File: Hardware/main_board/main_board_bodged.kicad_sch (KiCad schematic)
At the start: 116 parts, among them J1 ALARM, J2 RFID_CONN, J3 GPS_CONN, J4 USB_A, J5 DEBUG, J6 ANTENNA2, J7 Conn_01x04_Male, J8 BATT, SW1 SW_Push, SW2 SW_Push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

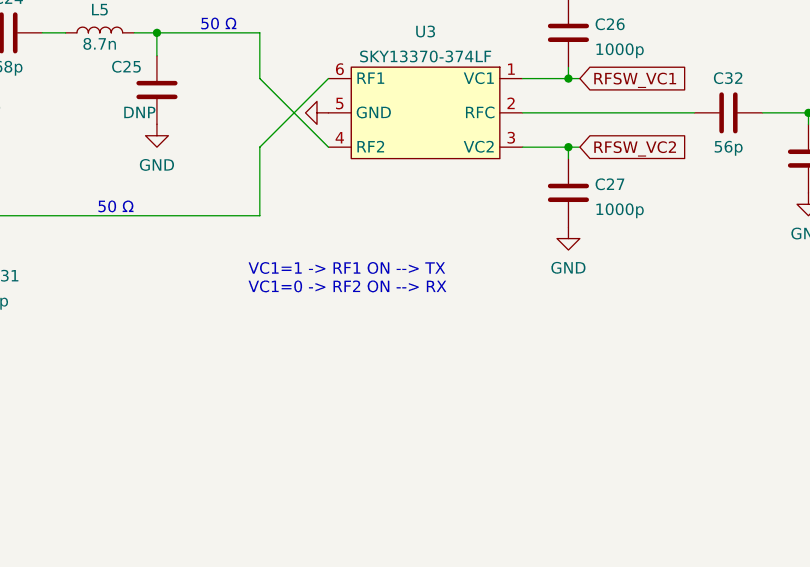
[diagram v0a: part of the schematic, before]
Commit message: lora helper functions
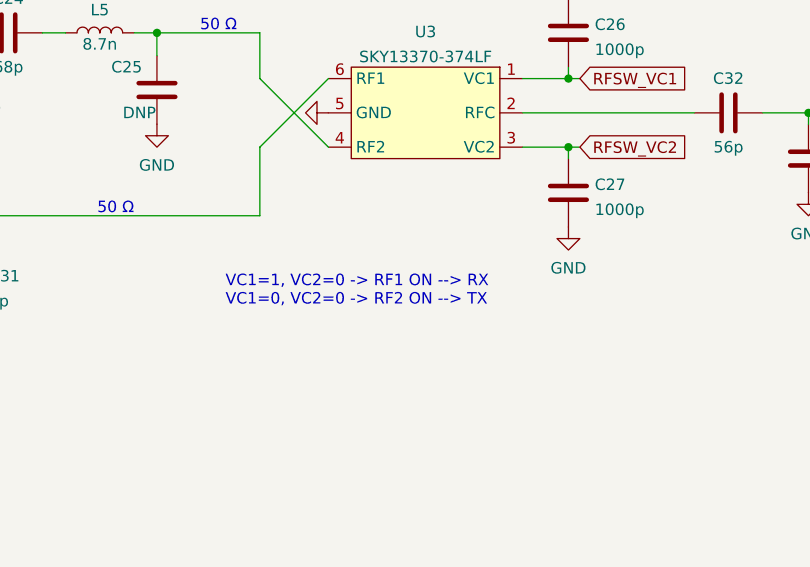
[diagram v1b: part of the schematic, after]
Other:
- note added: "VC1=1, VC2=0 -> RF1 ON --> RX VC1=0, VC2=0 -> RF2 ON --> TX"
- note removed: "VC1=1 -> RF1 ON --> TX VC1=0 -> RF2 ON --> RX"
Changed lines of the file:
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@@
     (effects (font (size 2 2) (thickness 0.4) bold italic) (justify left bottom))
   )
-  (text "VC1=1 -> RF1 ON --> TX \nVC1=0 -> RF2 ON --> RX\n" (at 190.5 114.3 0)
+  (text "VC1=1, VC2=0 -> RF1 ON --> RX\nVC1=0, VC2=0 -> RF2 ON --> TX\n"
+    (at 187.96 115.57 0)
     (effects (font (size 1.27 1.27)) (justify left bottom))
   )

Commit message: safety commit, uart working kinda
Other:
- note added: "PA8 (TP3): 32MHz master clock output"
- note added: "VC1=1, VC2=0 -> RF1 ON --> RX VC1=0, VC2=1 -> RF2 ON --> TX"
- note removed: "VC1=1, VC2=0 -> RF1 ON --> RX VC1=0, VC2=0 -> RF2 ON --> TX"
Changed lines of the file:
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@@
     (effects (font (size 2 2) (thickness 0.4) bold italic) (justify left bottom))
   )
-  (text "VC1=1, VC2=0 -> RF1 ON --> RX\nVC1=0, VC2=0 -> RF2 ON --> TX\n"
+  (text "VC1=1, VC2=0 -> RF1 ON --> RX\nVC1=0, VC2=1 -> RF2 ON --> TX\n"
     (at 187.96 115.57 0)
     (effects (font (size 1.27 1.27)) (justify left bottom))
@@
     (effects (font (size 1.27 1.27) italic) (justify left bottom))
   )
+  (text "PA8 (TP3): 32MHz master clock output" (at 38.1 156.21 0)
+    (effects (font (size 1.27 1.27)) (justify left bottom))
+  )
   (text "- This board assumes the high-power RF output configuration: \nthis means the output pin is RFO_HP, and VR_PA is tied to VCC. "

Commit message: hahahhah
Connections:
- net RFID_DATA0 is gone; now on net PA12: TP22.1, U1.35 (PA12)
- net PA12: now reaches J3.6 (Pin_6)
- net ALARM_ON renamed LPUART1_NTX
- net GPS_STATE renamed PA11
- net I2C1_SCL renamed PB8
- net I2C1_SDA renamed PB7
- net RFID_DATA1 renamed PA1
- net RFID_LED renamed NC
- net RFID_NRST renamed PB5
- net RFID_TAG_IN_RANGE renamed PA0
- net RFSW_VC1 renamed LPUART1_NRX
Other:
- note added: "IDLE LED: PB8 UNLOCKED LED: PA1 ALARM LED: PB5 TRANSIT LED: PA0"
- note added: "PA11 -- TIM1_CH4"
